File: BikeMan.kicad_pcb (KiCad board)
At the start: 2 copper layers, 90 x 99 mm, 127 parts, among them J1 Barrel_Jack, J11 PushConnector_8pos, J14 PushConnector_8pos, J2 Conn_01x12_Male, J3 Conn_01x06_Male, J4 MicroUSB, Q1 AUIRF7316QTR, Q2 AUIRF7316QTR, Q3 AUIRF7316QTR, Q4 AUIRF7316QTR, Q5 DMN62D0U-7, Q6 DMN62D0U-7, Q7 DMN62D0U-7, U1 AP64501, U10 PCF8574DWR, U2 MCP2551, U3 MCP2221A, U4 TCN75, U5 MCP2515, U6 ESP32, U7 PCF85063A, U8 NPIC6C596ADJ, U9 TPS79933, Y1 ABLS7M-16.000MHZ-B-2-T, Y3 Crystal-CM7V-T1A-32.768kHz

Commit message: WIP
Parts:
- added D20: LED_Green, LED_SMD:LED_0805_2012Metric_Pad1.15x1.40mm_HandSolder, F.Cu at (164.6, 118.0)
- added R35: R, Resistor_SMD:R_0805_2012Metric, B.Cu at (164.6, 118.0)
- moved TP2 128.3 mm to (72.0, 74.4)
- moved TP7 128.3 mm to (61.1, 73.1)
- moved TP8 128.3 mm to (61.1, 69.1)
- moved TP1 128.3 mm to (68.5, 74.4)
- moved TP3 128.3 mm to (58.6, 76.9)
- moved TP4 128.3 mm to (62.1, 76.9)
- moved TP5 128.3 mm to (65.0, 82.1)
- moved TP6 128.3 mm to (65.0, 79.1)
- moved D16 17.1 mm to (164.6, 115.3)
- moved R33 4.81 mm to (151.5, 133.8)
- moved R34 0.84 mm to (151.5, 131.8)
- moved R32 0.65 mm to (151.5, 127.6)
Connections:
- U3 pad 8: unconnected-(U3-Pad8) -> /MicroController/esp_reset
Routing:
- net +3V3: track 49.3 -> 201.7 mm, vias 3 -> 11
- net /MicroController/~silent_boot: track 0.00 -> 68.1 mm, vias 0 -> 7
- net /MicroController/bootmode_select: track 28.5 -> 92.4 mm, vias 2 -> 7
- net +5V: track 151.3 -> 200.0 mm, vias 7 -> 9
- net /MicroController/esp_reset: track 0.00 -> 19.8 mm, vias 0 -> 1
- net /MicroController/esp_rx: track 66.3 -> 79.1 mm, vias 0 -> 1
- net /USB.PWR: track 0.00 -> 9.39 mm
- net /SCL_{3.3V}: track 115.8 -> 123.9 mm, vias 4 -> 5
- net Net-(J2-Pad10): track 0.00 -> 7.40 mm
- net /SDA_{3.3V}: track 116.3 -> 123.7 mm, vias 4 -> 5
- net Net-(J2-Pad12): track 0.00 -> 6.71 mm
- net Net-(J2-Pad11): track 0.00 -> 3.35 mm
- net /MicroController/esp_tx: track 68.5 -> 71.6 mm, vias 0 -> 1
- net /GPIO/OUT_CTL_{7}: track 32.1 -> 34.7 mm
- net Net-(D20-Pad1): track 0.00 -> 2.21 mm, vias 0 -> 1
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
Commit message: finished routing
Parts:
- moved TP3 43.9 mm to (95.0, 101.4)
- moved TP7 42.8 mm to (103.8, 75.4)
- moved TP8 39.5 mm to (100.0, 75.8)
- moved TP4 37.5 mm to (98.4, 86.2)
- moved TP6 30.0 mm to (95.0, 80.0)
- moved TP5 28.2 mm to (93.2, 82.2)
- moved TP1 26.9 mm to (91.2, 60.0)
- moved TP2 20.9 mm to (89.2, 62.4)
- moved J3 1.60 mm to (83.7, 66.7)
- moved H1 0.90 mm to (84.6, 59.8)
- turned R31 to 0 degrees
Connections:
- J3 pad 1: +5V -> unconnected-(J3-Pad1)
- J3 pad 3: /CAN_{L} -> unconnected-(J3-Pad3)
- J3 pad 4: unconnected-(J3-Pad4) -> /CAN_{L}
- J3 pad 5: unconnected-(J3-Pad5) -> GND
- J3 pad 6: GND -> +5V
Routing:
- net /MicroController/esp_reset: track 19.8 -> 53.4 mm, vias 1 -> 2
- net +5V: track 200.0 -> 211.2 mm
- net /CAN Peripherals/OSC1: track 8.40 -> 16.3 mm, vias 0 -> 2
- net /CAN Peripherals/OSC2: track 8.43 -> 14.9 mm
- net /CAN_{L}: track 41.4 -> 46.9 mm
- net /CAN_{H}: track 40.7 -> 44.7 mm
- net /CAN Peripherals/~{reset}: track 5.01 -> 8.70 mm
- net Net-(D19-Pad1): track 0.00 -> 3.22 mm, vias 0 -> 1
- net /MicroController/~silent_boot: track 68.1 -> 69.0 mm
- net GND: track 100.9 -> 101.0 mm, vias 26 -> 29

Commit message: geographical reannotate
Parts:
- removed H4: MountingHole_Pad, MountingHole:MountingHole_3.2mm_M3
- moved H3 71.4 mm to (84.0, 107.0)
- moved TP7 1.71 mm to (105.2, 74.5)
- moved H1 0.63 mm to (84.0, 60.0)
- moved TP8 0.32 mm to (100.2, 76.0)
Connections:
- JP8 pad 2: Net-(JP8-Pad2) -> /CAN Peripherals/CAN_{Tx}
- U2 pad 1: Net-(JP8-Pad2) -> /CAN Peripherals/CAN_{Tx}
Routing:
- net /CAN Peripherals/CAN_{Tx}: track 0.00 -> 13.7 mm, vias 0 -> 2
- net Net-(JP8-Pad2): track 11.4 -> 0.00 mm, vias 2 -> 0
- net /CAN Peripherals/CAN_{RxLOW}: track 9.23 -> 12.7 mm
- net Net-(C20-Pad1): track 0.00 -> 2.92 mm, vias 0 -> 1
- net Net-(D11-Pad1): track 0.00 -> 2.56 mm, vias 0 -> 1
- net GND: track 101.0 -> 102.2 mm, vias 29 -> 54

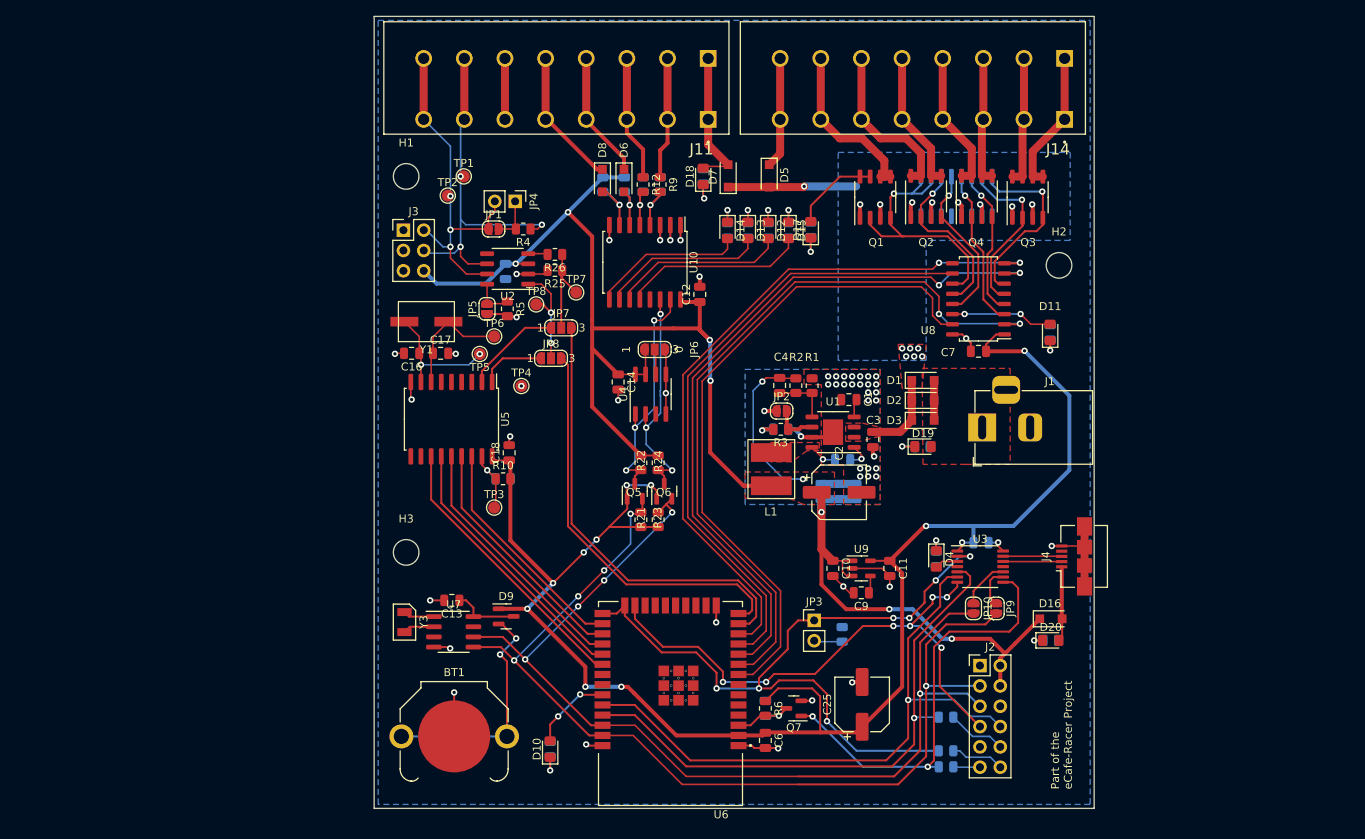
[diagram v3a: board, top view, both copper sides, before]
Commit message: added test points and cleaned up silk screen
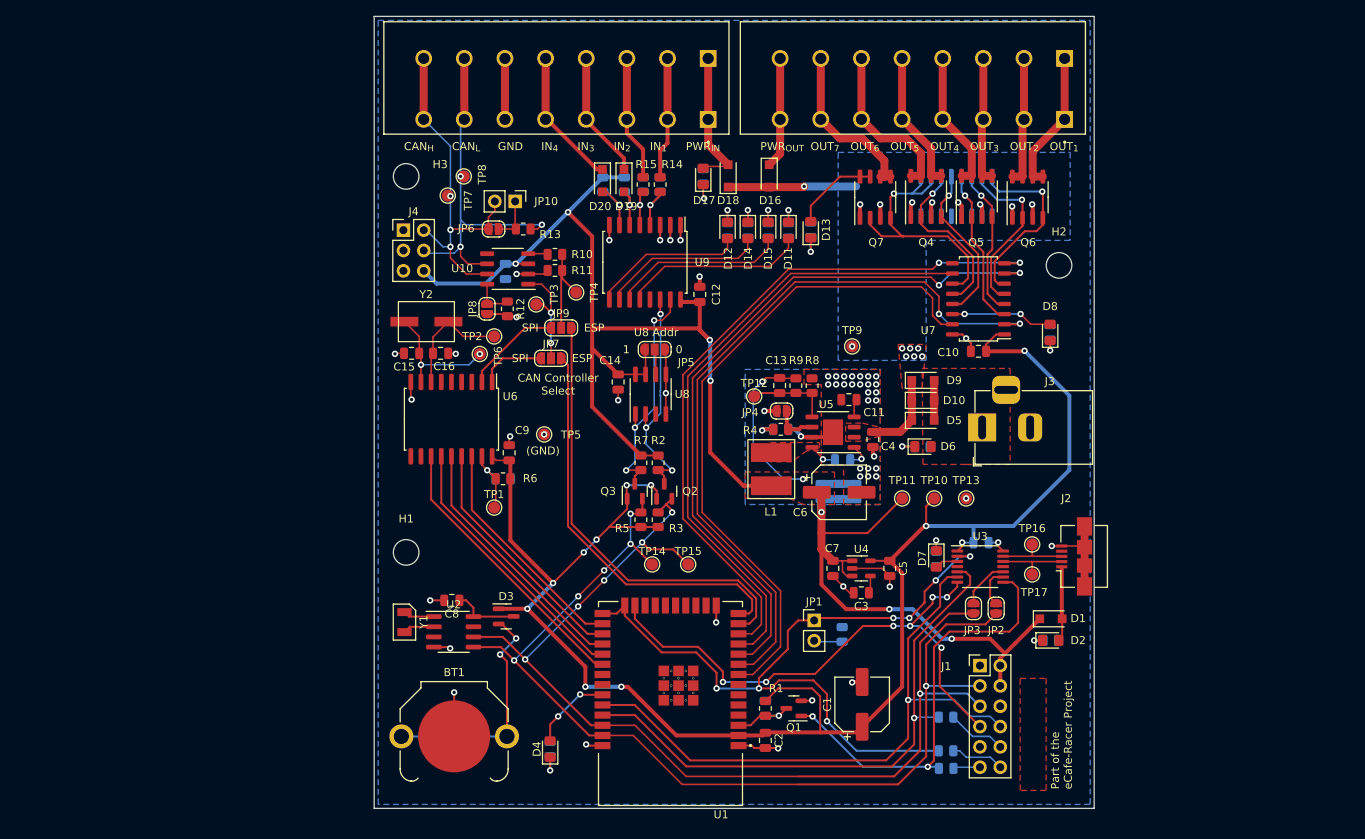
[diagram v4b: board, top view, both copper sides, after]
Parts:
- added TP10: TestPoint, TestPoint:TestPoint_Pad_D1.5mm, F.Cu at (150.0, 100.2)
- added TP11: TestPoint, TestPoint:TestPoint_Pad_D1.5mm, F.Cu at (146.0, 100.2)
- added TP12: TestPoint, TestPoint:TestPoint_Pad_D1.5mm, F.Cu at (127.5, 87.5)
- added TP13: TestPoint, TestPoint:TestPoint_Pad_D1.5mm, F.Cu at (154.0, 100.2)
- added TP14: TestPoint, TestPoint:TestPoint_Pad_D1.5mm, F.Cu at (114.8, 108.5)
- added TP15: TestPoint, TestPoint:TestPoint_Pad_D1.5mm, F.Cu at (119.2, 108.5)
- added TP16: TestPoint, TestPoint:TestPoint_Pad_D1.5mm, F.Cu at (162.2, 106.0)
- added TP17: TestPoint, TestPoint:TestPoint_Pad_D1.5mm, F.Cu at (162.2, 109.8)
- added TP9: TestPoint, TestPoint:TestPoint_Pad_D1.5mm, F.Cu at (139.8, 81.2)
- moved TP5 6.69 mm to (101.2, 92.2)
- moved R19 0.20 mm to (151.5, 134.0)
- renumbered C25 to C1, C7 to C10, C1 to C11, C4 to C13, C16 to C15, C17 to C16, C5 to C17, C15 to C18, C22 to C19, C6 to C2, C19 to C21, C23 to C22, C8 to C23, C21 to C24, C24 to C25, C9 to C3, C3 to C4, C11 to C5, C2 to C6, C10 to C7, C13 to C8, C18 to C9, D16 to D1, D2 to D10, D15 to D11, D14 to D12, D17 to D13, D13 to D14, D12 to D15, D5 to D16, D18 to D17, D7 to D18, D6 to D19, D20 to D2, D8 to D20, D9 to D3, D10 to D4, D3 to D5, D19 to D6, D4 to D7, D11 to D8, D1 to D9, H3 to H1, H1 to H3, J2 to J1, J4 to J2, J1 to J3, J3 to J4, J14 to J5, J11 to J6, JP3 to JP1, JP4 to JP10, JP9 to JP2, JP10 to JP3, JP2 to JP4, JP6 to JP5, JP1 to JP6, JP8 to JP7, JP5 to JP8, JP7 to JP9, Q7 to Q1, Q6 to Q2, Q5 to Q3, Q2 to Q4, Q4 to Q5, Q3 to Q6, Q1 to Q7, R6 to R1, R26 to R10, R25 to R11, R5 to R12, R4 to R13, R9 to R14, R12 to R15, R8 to R16, R28 to R17, R34 to R18, R33 to R19, R24 to R2, R35 to R20, R32 to R21, R31 to R22, R7 to R23, R17 to R24, R29 to R25, R27 to R26, R20 to R27, R18 to R28, R16 to R29, R23 to R3, R15 to R30, R14 to R31, R13 to R32, R30 to R33, R11 to R34, R19 to R35, R3 to R4, R21 to R5, R10 to R6, R22 to R7, R1 to R8, R2 to R9, TP3 to TP1, TP6 to TP2, TP8 to TP3, TP7 to TP4, TP4 to TP5, TP5 to TP6, TP2 to TP7, TP1 to TP8, U6 to U1, U2 to U10, U7 to U2, U9 to U4, U1 to U5, U5 to U6, U8 to U7, U4 to U8, U10 to U9, Y3 to Y1, Y1 to Y2
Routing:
- net +5V: track 211.2 -> 223.1 mm
- net /SCL_{3.3V}: track 123.9 -> 130.8 mm, vias 5 -> 6
- net +3V3: track 201.7 -> 205.6 mm
- net /SDA_{3.3V}: track 123.7 -> 127.5 mm, vias 5 -> 6
- net /Power Supply/feedback: track 7.08 -> 10.4 mm
- net /USB.-: track 7.31 -> 8.95 mm
- net /USB.+: track 7.21 -> 8.70 mm
- net GND: vias 54 -> 55
- net +12V: vias 15 -> 16
- added copper zone on F.Cu, net (none)
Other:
- board text added: "(GND)"
- board text added: "CAN Controller Select"
- board text added: "CAN_{H}"
- board text added: "CAN_{L}"
- board text added: "GND"
- board text added: "IN_{1}"
- board text added: "IN_{2}"
- board text added: "IN_{3}"
- board text added: "IN_{4}"
- board text added: "OUT_{1}"
- board text added: "OUT_{2}"
- board text added: "OUT_{3}"
- board text added: "OUT_{4}"
- board text added: "OUT_{5}"
- board text added: "OUT_{6}"
- board text added: "OUT_{7}"
- board text added: "PWR_{IN}"
- board text added: "PWR_{OUT}"
- board text added: "U8 Addr"

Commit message: updated 3d models
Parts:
- J5, J6: footprint footprints:CUI_TBL004-508-08BE-2BE -> ecafe-racer:CUI_TBL004-508-08BE-2BE
- Q4, Q5, Q6, Q7: footprint Package_SO:SO-8_3.9x4.9mm_P1.27mm -> ecafe-racer:SO-8_3.9x4.9mm_P1.27mm
- moved H2 0.62 mm to (165.0, 71.0)
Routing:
- net /SDA_{3.3V}: track 127.5 -> 126.9 mm
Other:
- board text added: "github.com/eCafe-Racer/Dennis"

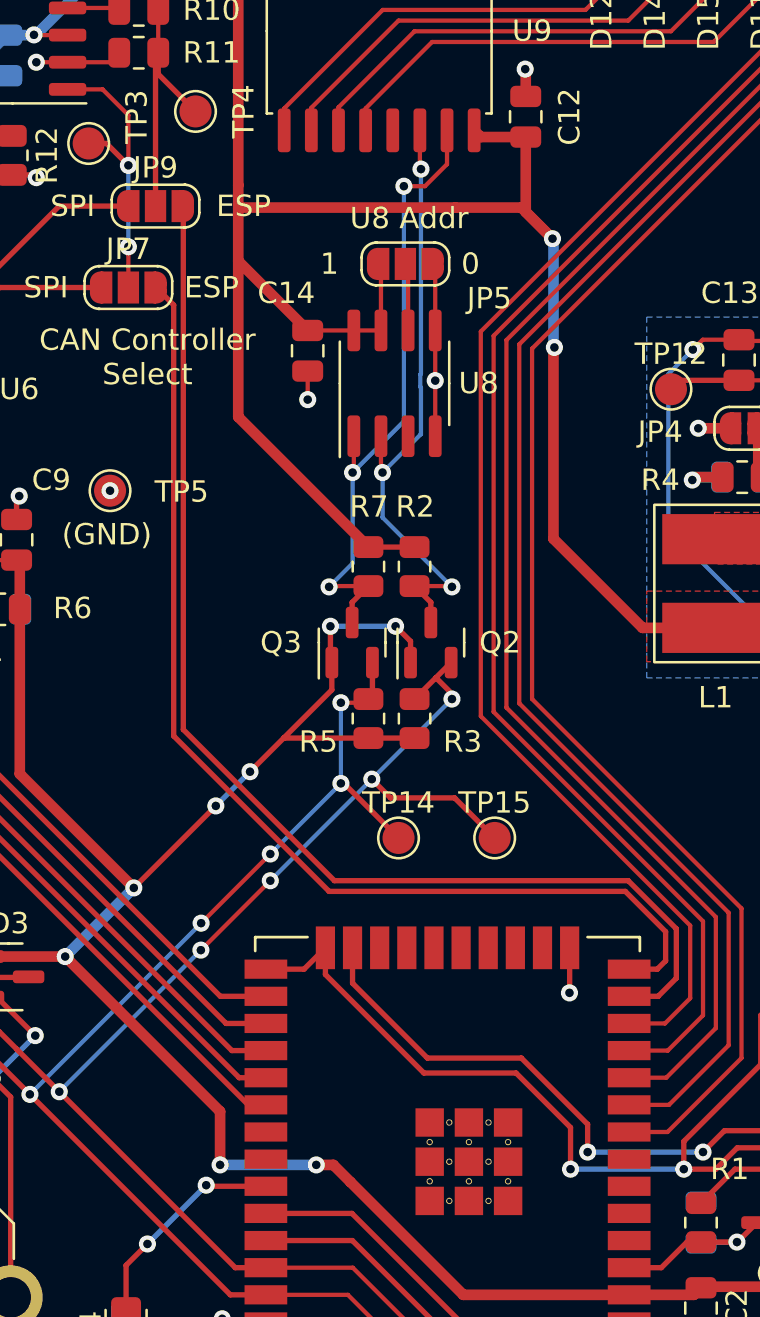
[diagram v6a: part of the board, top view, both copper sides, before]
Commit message: Forgot to connect the interrupt signal for the GPIO
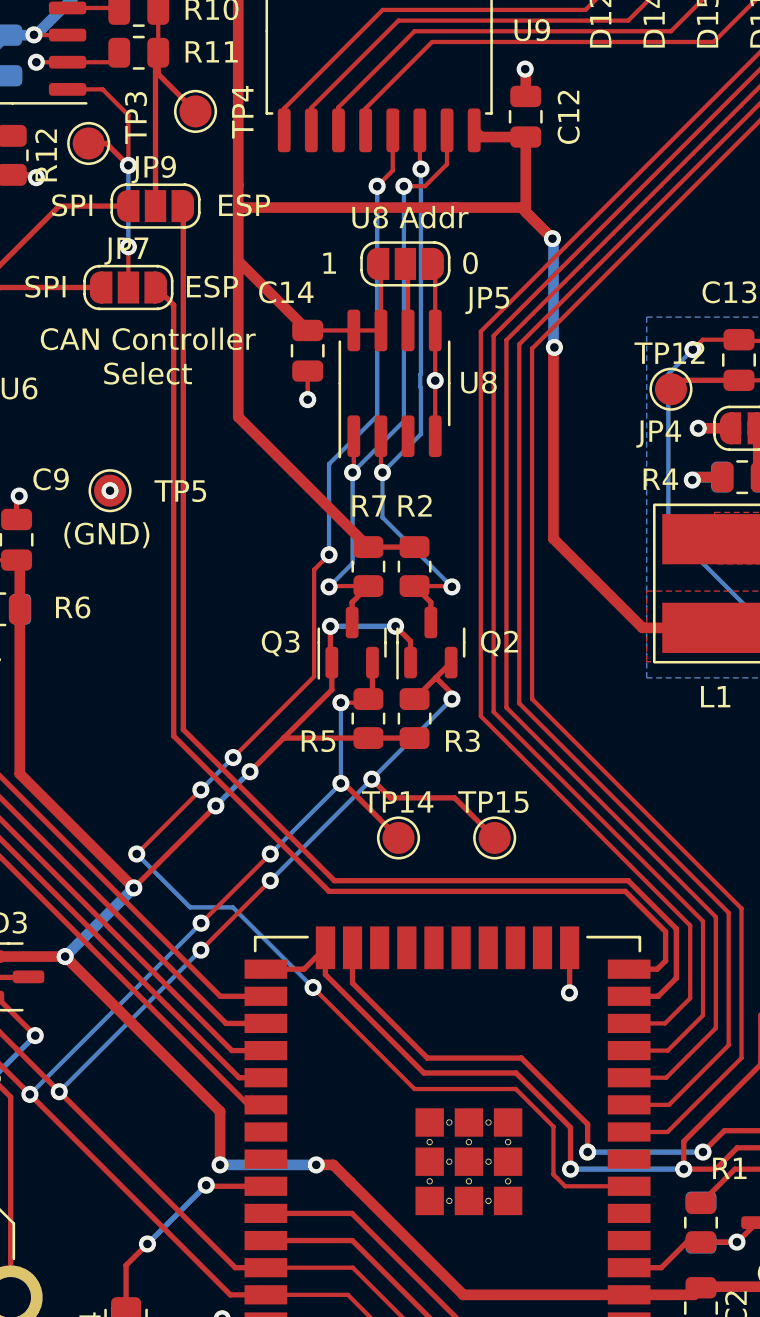
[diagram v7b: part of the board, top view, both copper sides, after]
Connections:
- net /GPIO/OUT_{1} renamed /Output_{1}
- net /GPIO/OUT_{2} renamed /Output_{2}
- net /GPIO/OUT_{3} renamed /Output_{3}
- net /GPIO/OUT_{4} renamed /Output_{4}
- net /GPIO/OUT_{5} renamed /Output_{5}
- net /GPIO/OUT_{6} renamed /Output_{6}
- net /GPIO/OUT_{7} renamed /Output_{7}
- net /Power Supply/PWR_IN renamed /Jack_PWR
- C13 pad 1: +5V -> /Power Supply/Vout
- R9 pad 1: +5V -> /Power Supply/Vout
- U1 pad 6: unconnected-(U1-Pad6) -> /~{INT_{GPIO}}
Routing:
- net /~{INT_{GPIO}}: track 0.00 -> 69.6 mm, vias 0 -> 6
- net /Power Supply/Vout: track 0.00 -> 21.1 mm, vias 0 -> 2
- net +5V: track 223.1 -> 202.0 mm, vias 9 -> 7
